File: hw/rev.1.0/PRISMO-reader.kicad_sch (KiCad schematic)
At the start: 48 parts, among them J1 Conn_01x03, J3 PN532 Connector, J4 External 5V power, J5 USB4120-03-C_REVA, K1 G5LE-1, Q1 2N7002, Q2 BC847, Q3 BC847, SW1 Logout button, U1 ESP32-WROOM-32D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

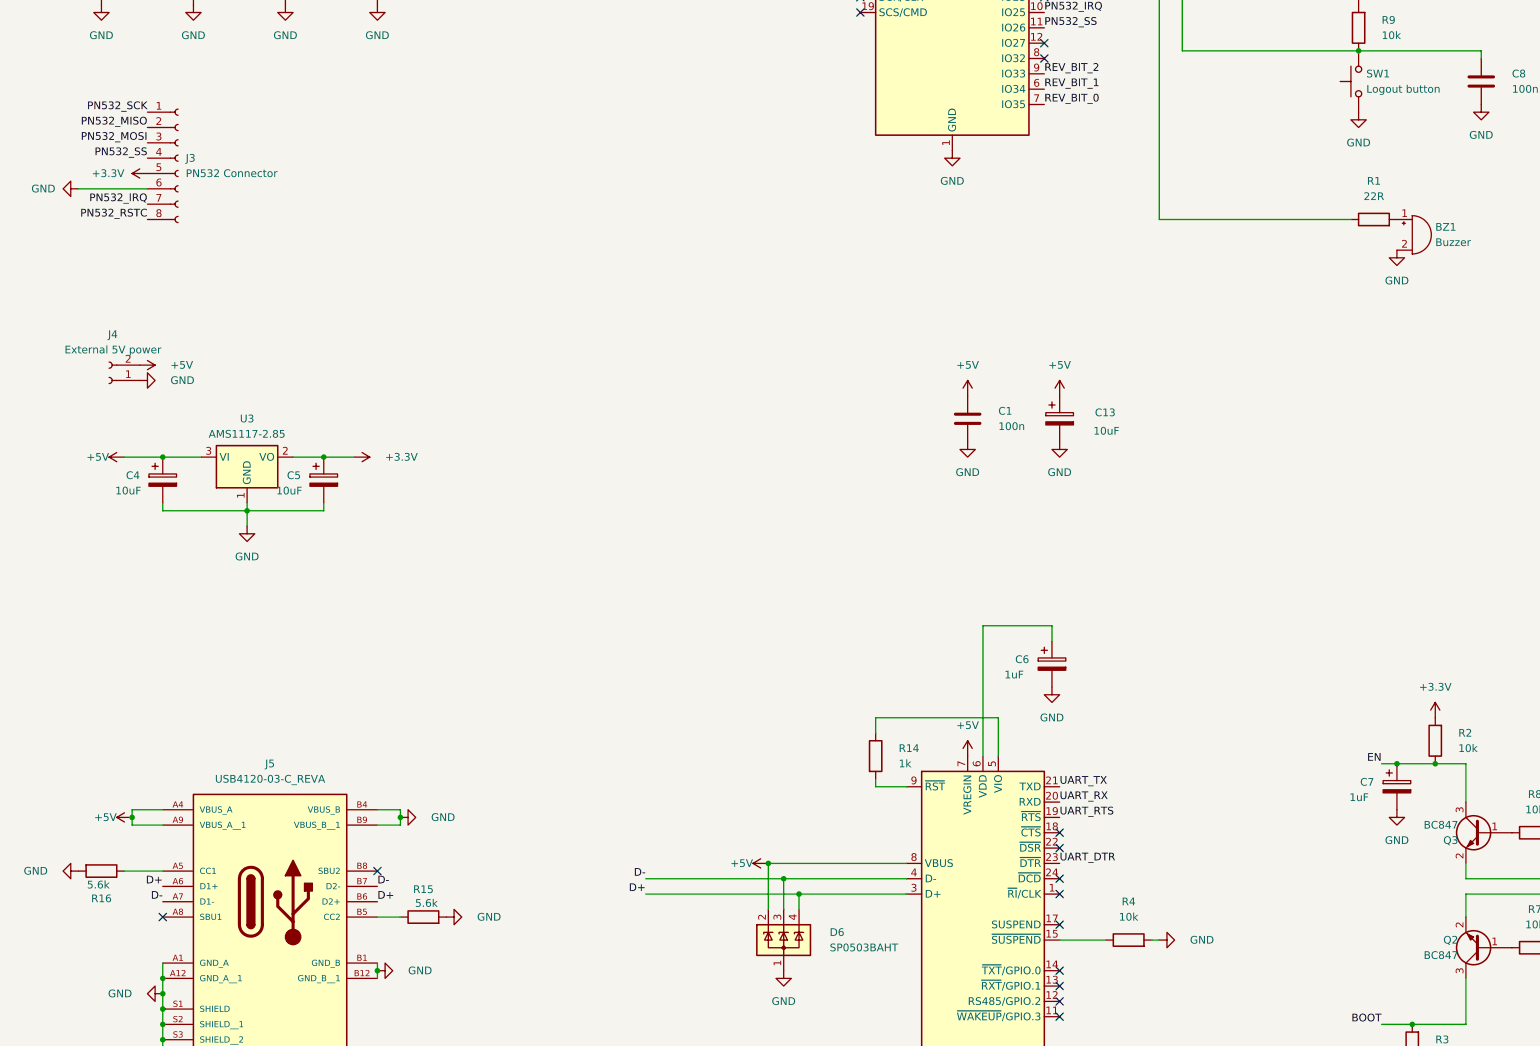
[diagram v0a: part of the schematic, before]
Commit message: Fixed problem with wrong VBUS connection of USB port
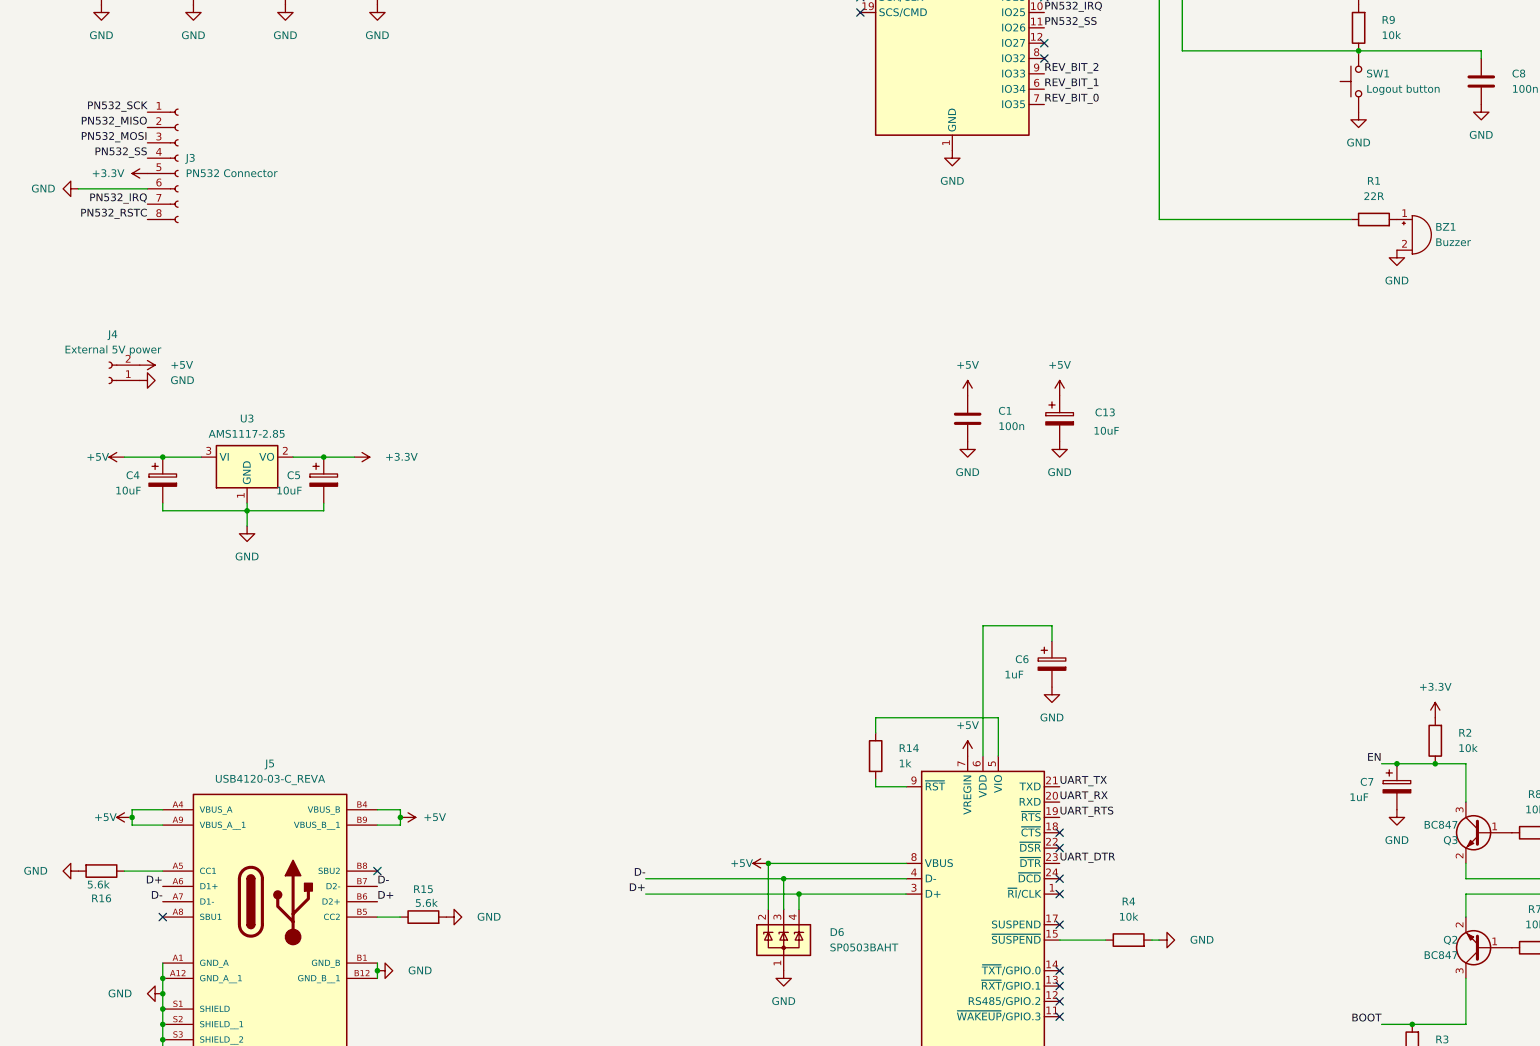
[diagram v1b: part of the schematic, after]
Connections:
- net +5V: now also J5.B4 (VBUS_B), J5.B9 (VBUS_B__1)
- net GND: no longer J5.B4 (VBUS_B), J5.B9 (VBUS_B__1)
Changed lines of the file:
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@@
 (kicad_sch
-	(version 20231120)
+	(version 20240417)
 	(generator "eeschema")
-	(generator_version "8.0")
+	(generator_version "8.99")
 	(paper "A3")
 	(title_block
@@
 		(comment 1 "Authors: Artem Synytsyn <a,synytsyn@gmail.com>, Oleksandr Ivanchuk aka Sashkoiv")
 	)
-	(junction
-		(at 254 205.74)
-		(diameter 0)
-		(color 0 0 0 0)
+	(text "       REVISION CODE: \n     |BIT0 | BIT1 | BIT2\n     |==================\n1.0  |  1  |   1  |  1"
+		(exclude_from_sim no)
+		(at 370.078 205.994 0)
+		(effects
+			(font
+				(size 1.27 1.27)
+			)
+		)
 	)
 	(junction
-		(at 88.9 214.63)
+		(at 254 205.74)
 		(diameter 0)
 		(color 0 0 0 0)
@@
 	)
 	(junction
+		(at 88.9 214.63)
+		(diameter 0)
+		(color 0 0 0 0)
+	)
+	(junction
 		(at 247.65 46.99)
 		(diameter 0)
@@
 	(wire
 		(pts
+			(xy 88.9 214.63) (xy 88.9 215.9)
+		)
+		(stroke
+			(width 0)
+			(type default)
+		)
+	)
+	(wire
+		(pts
 			(xy 195.58 68.58) (xy 218.44 68.58)
 		)
@@
 	(wire
 		(pts
-			(xy 88.9 214.63) (xy 88.9 215.9)
-		)
-		(stroke
-			(width 0)
-			(type default)
-		)
-	)
-	(wire
-		(pts
 			(xy 359.41 179.07) (xy 358.14 179.07)
 		)
@@
 		)
 	)
-	(text "       REVISION CODE: \n     |BIT0 | BIT1 | BIT2\n     |==================\n1.0  |  1  |   1  |  1"
-		(exclude_from_sim no)
-		(at 370.078 205.994 0)
-		(effects
-			(font
-				(size 1.27 1.27)
-			)
-		)
-	)
 	(label "D+"
 		(at 129.54 227.33 180)
@@
 	)
 	(symbol
-		(lib_id "power:GND")
-		(at 88.9 214.63 90)
-		(unit 1)
-		(exclude_from_sim no)
-		(in_bom yes)
-		(on_board yes)
-		(dnp no)
-		(fields_autoplaced yes)
-		(property "Reference" "#PWR058"
-			(at 95.25 214.63 0)
-			(effects
-				(font
-					(size 1.27 1.27)
-				)
-				(hide yes)
-			)
-		)
-		(property "Value" "GND"
-			(at 93.98 214.6299 90)
-			(effects
-				(font
-					(size 1.27 1.27)
-				)
-				(justify right)
-			)
-		)
-		(property "Footprint" ""
-			(at 88.9 214.63 0)
-			(effects
-				(font
-					(size 1.27 1.27)
-				)
-				(hide yes)
-			)
-		)
-		(property "Datasheet" ""
-			(at 88.9 214.63 0)
-			(effects
-				(font
-					(size 1.27 1.27)
-				)
-				(hide yes)
-			)
-		)
-		(property "Description" "Power symbol creates a global label with name \"GND\" , ground"
-			(at 88.9 214.63 0)
-			(effects
-				(font
-					(size 1.27 1.27)
-				)
-				(hide yes)
-			)
-		)
-		(pin "1"
-		)
-		(instances
-			(project "PRISMO-reader"
-				(path "/2a3560c2-ed74-4b68-8cf6-2c43628355c3"
-					(reference "#PWR058")
-					(unit 1)
-				)
-			)
-		)
-	)
-	(symbol
 		(lib_id "power:+5V")
 		(at 45.72 139.7 270)
@@
 					(unit 1)
 				)
+			)
+		)
+	)
+	(symbol
+		(lib_id "power:+5V")
+		(at 88.9 214.63 270)
+		(unit 1)
+		(exclude_from_sim no)
+		(in_bom yes)
+		(on_board yes)
+		(dnp no)
+		(fields_autoplaced yes)
+		(property "Reference" "#PWR06"
+			(at 85.09 214.63 0)
+			(effects
+				(font
+					(size 1.27 1.27)
+				)
+				(hide yes)
+			)
+		)
+		(property "Value" "+5V"
+			(at 92.71 214.6299 90)
+			(effects
+				(font
+					(size 1.27 1.27)
+				)
+				(justify left)
+			)
+		)
+		(property "Footprint" ""
+			(at 88.9 214.63 0)
+			(effects
+				(font
+					(size 1.27 1.27)
+				)
+				(hide yes)
+			)
+		)
+		(property "Datasheet" ""
+			(at 88.9 214.63 0)
+			(effects
+				(font
+					(size 1.27 1.27)
+				)
+				(hide yes)
+			)
+		)
+		(property "Description" "Power symbol creates a global label with name \"+5V\""
+			(at 88.9 214.63 0)
+			(effects
+				(font
+					(size 1.27 1.27)
+				)
+				(hide yes)
+			)
+		)
+		(pin "1"
+		)
+		(instances
+			(project "PRISMO-reader"
+				(path "/2a3560c2-ed74-4b68-8cf6-2c43628355c3"
+					(reference "#PWR06")
+					(unit 1)
+				)

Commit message: Bugfix with CP2102 connection (#15)
* fixed CP2102 peripheral connection

* renamed leds in order of connection
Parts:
- removed R4: 10k, Resistor_SMD:R_0805_2012Metric_Pad1.20x1.40mm_HandSolder, symbol Device:R
- R14: value 1k -> 10k
- renumbered D3 to D1, D4 to D2, D2 to D3, D1 to D4
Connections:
- net +5V: now also R14.1
- net at U2.5 (VIO): no longer R14.1
- no-connect marks 28 -> 30
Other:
- moved on the sheet: R14
